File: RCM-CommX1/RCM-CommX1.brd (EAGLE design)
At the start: 50.8 x 66 mm, 23 parts, among them J1 BLACKFIN_HEADER, U1 MATCHPORT

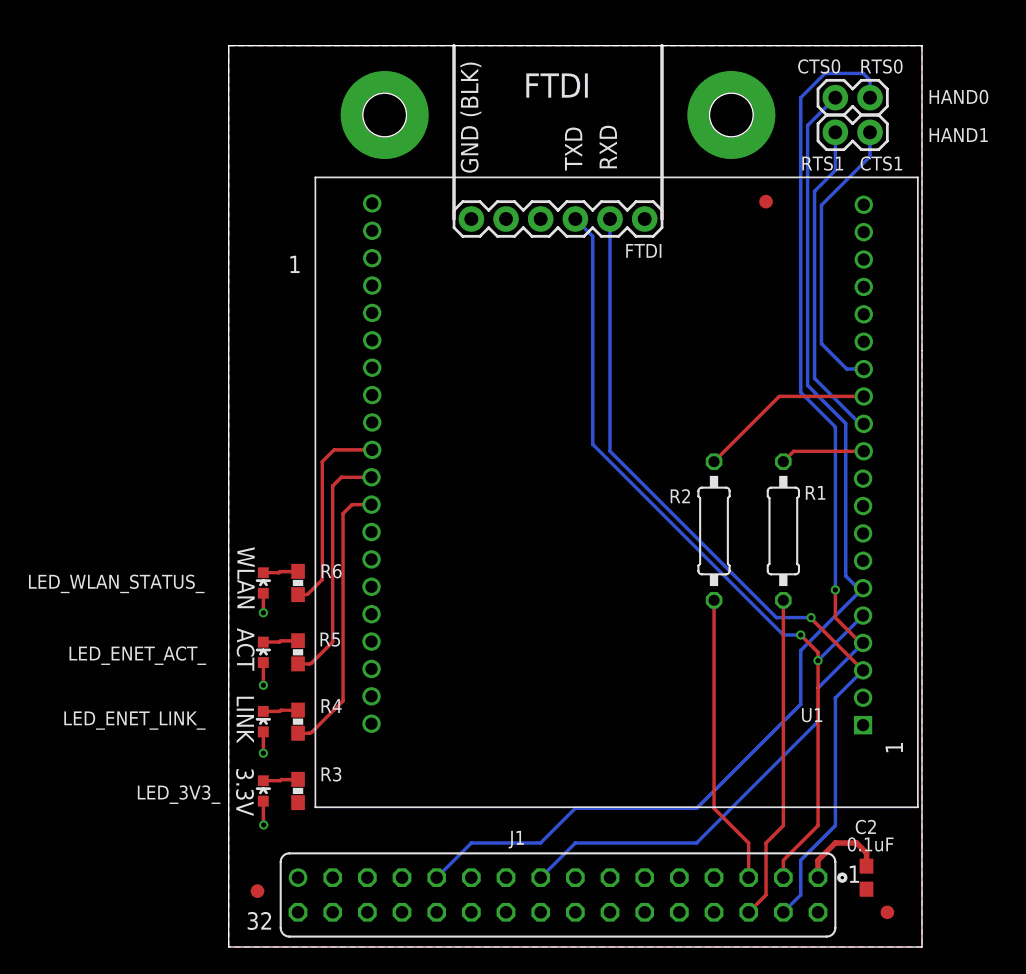
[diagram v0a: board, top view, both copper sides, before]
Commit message: Started xPico version of RCM-Comm board.
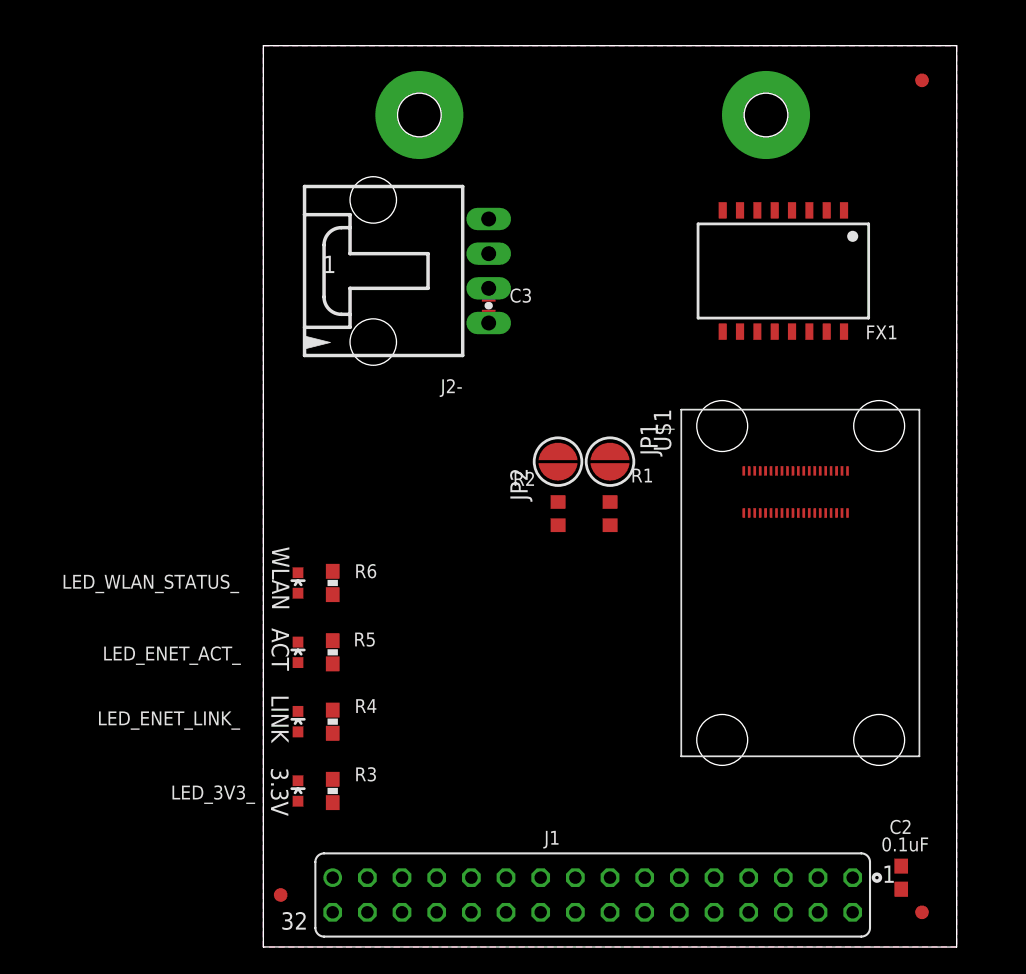
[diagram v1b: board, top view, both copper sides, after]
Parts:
- removed FTDI: (no value), spark_fun:1X06
- removed HAND0, HAND1: (no value), spark_fun:1X02
- removed U1: MATCHPORT, Matchport_Wiport:MATCHPORT_LAYOUT
- added C3: 1000pF, spark_fun:0603-CAP
- added FX1: S558-5999-T7-F, halo-electronics:N5
- added J2-: C-GRID-04, MolexConnector:70555-04
- added JP1, JP2: JUMPER-PAD-2-NOROUND, SparkFun-Passives:PAD-JUMPER-2-NO_YES_SILK_ROUND
- added U$1: LANTRONIX_XPICO, xPico:LANTRONIX_XPICO
- R1, R2: device rcl:0207/10 -> rcl:R0603
- moved U$3 41.9 mm to (81.3, 16.5)
- moved LOGO1 33.4 mm to (63.5, 15.2)
- moved FID2 14.5 mm to (50.8, 63.5)
- moved R1 12.8 mm to (27.9, 31.8)
- moved R2 11.5 mm to (24.1, 31.8)
- moved C2 2.54 mm to (49.3, 5.08)
- moved U$8 2.54 mm to (14.0, 61.0)
- moved LED_3V3_ 2.54 mm to (5.08, 11.4)
- moved LED_ENET_ACT_ 2.54 mm to (5.08, 21.6)
- moved LED_ENET_LINK_ 2.54 mm to (5.08, 16.5)
- moved LED_WLAN_STATUS_ 2.54 mm to (5.08, 26.7)
- moved R3 2.54 mm to (7.62, 11.4)
- moved R4 2.54 mm to (7.62, 16.5)
- moved R5 2.54 mm to (7.62, 21.6)
- moved R6 2.54 mm to (7.62, 26.7)
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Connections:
- removed net CTS0: HAND0.2, J1.23, U1.11
- removed net RTS0: HAND0.1, J1.17, U1.7
- removed net RXD0: FTDI.3, J1.3, U1.9
- removed net TXD0: FTDI.2, J1.4, U1.5
- new net ERCT: FX1.10, U$1.P18
- new net ETCT: FX1.15, U$1.P12
- new net N$1: C3.1, FX1.2, FX1.7
- new net N$13: FX1.16, U$1.P13
- new net N$14: FX1.14, U$1.P11
- new net N$16: FX1.11, U$1.P19
- new net N$17: FX1.9, U$1.P17
- new net N$18: FX1.1, J2-.4
- new net N$19: FX1.3, J2-.3
- new net N$2: JP1.2, R1.1
- new net N$20: FX1.8, J2-.1
- new net N$21: FX1.6, J2-.2
- new net N$4: JP2.1, R2.1
- new net N$7: U$1.P6
- new net RXD2: JP2.2, U$1.P23
- new net TXD2: JP1.1, U$1.P25
- net ACT: now also U$1.P8; no longer U1.20
- net CTS1: now also J1.23, U$1.P16; no longer HAND1.2, U1.27
- net GND: now also C3.2, U$1.P1, U$1.P15, U$1.P2, U$1.P21, U$1.P37, U$1.P39, U$1.P40, U$1.P9; no longer FTDI.6, U1.2, U1.39
- net LINK: no longer U1.18
- net RTS1: now also J1.17, U$1.P5; no longer HAND1.1, U1.23
- net RXD1: now also J1.3, U$1.P7; no longer R2.1, U1.25
- net TXD1: now also J1.4, U$1.P10; no longer R1.1, U1.21
- net VCC: now also U$1.P29, U$1.P31, U$1.P33; no longer U1.37
- net WLAN: now also U$1.P4; no longer U1.22
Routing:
- net RTS0: track 81.4 -> 0.00 mm, vias 1 -> 0
- net CTS0: track 81.0 -> 0.00 mm
- net TXD0: track 62.4 -> 0.00 mm, vias 1 -> 0
- net RXD0: track 62.1 -> 0.00 mm, vias 2 -> 0
- net N$24: track 23.9 -> 0.00 mm
- net RTS1: track 23.7 -> 0.00 mm
- net N$26: track 21.4 -> 0.00 mm
- net CTS1: track 20.8 -> 0.00 mm
- net LINK: track 20.3 -> 0.00 mm
- net ACT: track 17.7 -> 0.00 mm
- net WLAN: track 14.9 -> 0.00 mm
- net VCC: track 13.5 -> 0.00 mm, vias 4 -> 0
- net RXD1: track 13.0 -> 0.00 mm
- net TXD1: track 6.21 -> 0.00 mm
- net N$6: track 2.58 -> 0.00 mm
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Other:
- board text removed: "CTS0"
- board text removed: "CTS1"
- board text removed: "FTDI"
- board text removed: "GND (BLK)"
- board text removed: "RTS0"
- board text removed: "RTS1"
- board text removed: "RXD"
- board text removed: "TXD"
